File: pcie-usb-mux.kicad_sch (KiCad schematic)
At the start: 7 parts, among them U16 TMUXHS4212IRKSR

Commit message: [#83609] Reannotate board
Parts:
- renumbered C39 to C19, C40 to C20, C41 to C21, R159 to R95, R48 to R96, R49 to R97, U16 to U5
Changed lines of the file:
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@@
 		(on_board yes)
 		(dnp no)
-		(property "Reference" "#PWR068"
+		(property "Reference" "#PWR041"
 			(at 195.58 107.95 0)
 			(effects
@@
 			(project "bmc-reference-carrier-board"
 				(path "/5f636c45-3c15-4731-8931-4625e0dab7e4/02dc288a-88ee-45fa-83b7-00b3500b0ccd"
-					(reference "#PWR068")
+					(reference "#PWR041")
 					(unit 1)
 				)
@@
 		(on_board yes)
 		(dnp no)
-		(property "Reference" "#PWR070"
+		(property "Reference" "#PWR042"
 			(at 199.39 158.75 0)
 			(effects
@@
 			(project "bmc-reference-carrier-board"
 				(path "/5f636c45-3c15-4731-8931-4625e0dab7e4/02dc288a-88ee-45fa-83b7-00b3500b0ccd"
-					(reference "#PWR070")
+					(reference "#PWR042")
 					(unit 1)
 				)
@@
 		(on_board yes)
 		(dnp no)
-		(property "Reference" "#PWR066"
+		(property "Reference" "#PWR038"
 			(at 176.53 107.95 0)
 			(effects
@@
 			(project "bmc-reference-carrier-board"
 				(path "/5f636c45-3c15-4731-8931-4625e0dab7e4/02dc288a-88ee-45fa-83b7-00b3500b0ccd"
-					(reference "#PWR066")
+					(reference "#PWR038")
 					(unit 1)
 				)
@@
 		(on_board yes)
 		(dnp no)
-		(property "Reference" "#PWR069"
+		(property "Reference" "#PWR040"
 			(at 189.23 158.75 0)
 			(effects
@@
 			(project "bmc-reference-carrier-board"
 				(path "/5f636c45-3c15-4731-8931-4625e0dab7e4/02dc288a-88ee-45fa-83b7-00b3500b0ccd"
-					(reference "#PWR069")
+					(reference "#PWR040")
 					(unit 1)
 				)
@@
 		(dnp no)
 		(fields_autoplaced yes)
-		(property "Reference" "U16"
+		(property "Reference" "U5"
 			(at 209.55 105.41 0)
 			(effects
@@
 			(project ""
 				(path "/5f636c45-3c15-4731-8931-4625e0dab7e4/02dc288a-88ee-45fa-83b7-00b3500b0ccd"
-					(reference "U16")
+					(reference "U5")
 					(unit 1)
 				)
@@
 		(on_board yes)
 		(dnp no)
-		(property "Reference" "#PWR065"
+		(property "Reference" "#PWR043"
 			(at 213.36 149.86 0)
 			(effects
@@
 			(project ""
 				(path "/5f636c45-3c15-4731-8931-4625e0dab7e4/02dc288a-88ee-45fa-83b7-00b3500b0ccd"
-					(reference "#PWR065")
+					(reference "#PWR043")
 					(unit 1)
 				)
@@
 		(dnp no)
 		(fields_autoplaced yes)
-		(property "Reference" "C39"
+		(property "Reference" "C19"
 			(at 170.18 100.3236 90)
 			(effects
@@
 			(project ""
 				(path "/5f636c45-3c15-4731-8931-4625e0dab7e4/02dc288a-88ee-45fa-83b7-00b3500b0ccd"
-					(reference "C39")
+					(reference "C19")
 					(unit 1)
 				)
@@
 		(on_board yes)
 		(dnp no)
-		(property "Reference" "#PWR067"
+		(property "Reference" "#PWR039"
 			(at 186.69 107.95 0)
 			(effects
@@
 			(project "bmc-reference-carrier-board"
 				(path "/5f636c45-3c15-4731-8931-4625e0dab7e4/02dc288a-88ee-45fa-83b7-00b3500b0ccd"
-					(reference "#PWR067")
+					(reference "#PWR039")
 					(unit 1)
 				)
@@
 		(dnp no)
 		(fields_autoplaced yes)
-		(property "Reference" "C41"
+		(property "Reference" "C21"
 			(at 189.23 100.3236 90)
 			(effects
@@
 			(project "bmc-reference-carrier-board"
 				(path "/5f636c45-3c15-4731-8931-4625e0dab7e4/02dc288a-88ee-45fa-83b7-00b3500b0ccd"
-					(reference "C41")
+					(reference "C21")
 					(unit 1)
 				)
@@
 		(dnp no)
 		(fields_autoplaced yes)
-		(property "Reference" "C40"
+		(property "Reference" "C20"
 			(at 180.34 100.3236 90)
 			(effects
@@
 			(project "bmc-reference-carrier-board"
 				(path "/5f636c45-3c15-4731-8931-4625e0dab7e4/02dc288a-88ee-45fa-83b7-00b3500b0ccd"
-					(reference "C40")
+					(reference "C20")
 					(unit 1)
 				)
@@
 		(dnp no)
 		(fields_autoplaced yes)
-		(property "Reference" "#PWR0201"
+		(property "Reference" "#PWR037"
 			(at 182.88 96.52 0)
 			(effects
@@
 			(project ""
 				(path "/5f636c45-3c15-4731-8931-4625e0dab7e4/02dc288a-88ee-45fa-83b7-00b3500b0ccd"
-					(reference "#PWR0201")
+					(reference "#PWR037")
 					(unit 1)
 				)
@@
 		(on_board yes)
 		(dnp no)
-		(property "Reference" "R159"
+		(property "Reference" "R95"
 			(at 170.815 142.24 0)
 			(effects
@@
 			(project ""
 				(path "/5f636c45-3c15-4731-8931-4625e0dab7e4/02dc288a-88ee-45fa-83b7-00b3500b0ccd"
-					(reference "R159")
+					(reference "R95")
 					(unit 1)
 				)
@@
 		(on_board yes)
 		(dnp no)
-		(property "Reference" "R49"
+		(property "Reference" "R97"
 			(at 191.77 151.13 90)
 			(effects
@@
 			(project "bmc-reference-carrier-board"
 				(path "/5f636c45-3c15-4731-8931-4625e0dab7e4/02dc288a-88ee-45fa-83b7-00b3500b0ccd"
-					(reference "R49")
+					(reference "R97")
 					(unit 1)
 				)
@@
 		(on_board yes)
 		(dnp no)
-		(property "Reference" "R48"
+		(property "Reference" "R96"
 			(at 181.864 151.13 90)
 			(effects
@@
 			(project ""
 				(path "/5f636c45-3c15-4731-8931-4625e0dab7e4/02dc288a-88ee-45fa-83b7-00b3500b0ccd"
-					(reference "R48")
+					(reference "R96")
 					(unit 1)
 				)

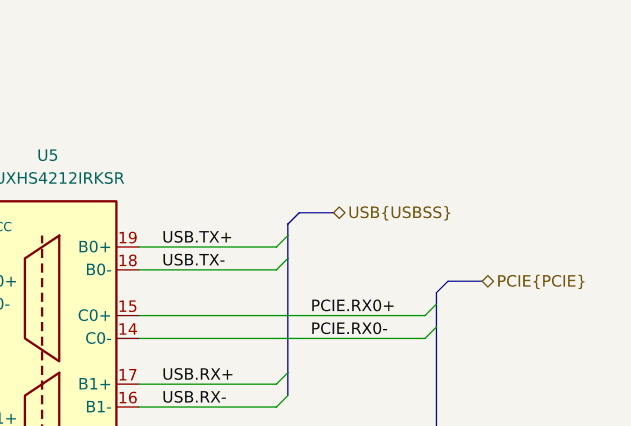
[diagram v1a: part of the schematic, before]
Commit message: [#83767] Add USB SS RX/TX swap note
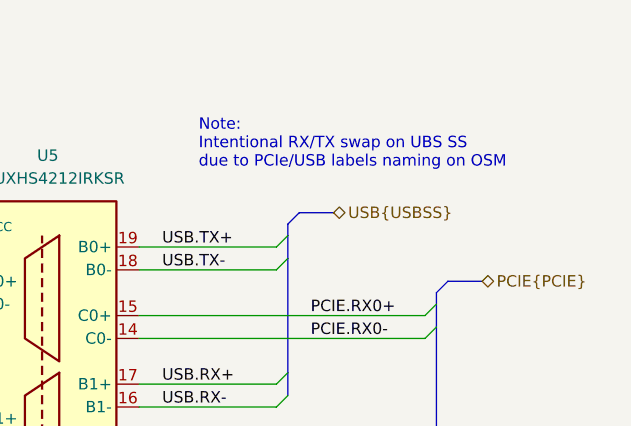
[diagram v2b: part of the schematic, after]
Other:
- note added: "Note: Intentional RX/TX swap on UBS SS due to PCIe/USB labels naming on OSM"
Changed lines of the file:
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@@
 		(rev "1.0.0")
+	)
+	(text "Note:\nIntentional RX/TX swap on UBS SS\ndue to PCIe/USB labels naming on OSM"
+		(exclude_from_sim no)
+		(at 226.314 104.14 0)
+		(effects
+			(font
+				(size 1.27 1.27)
+			)
+			(justify left)
+		)
 	)
 	(junction

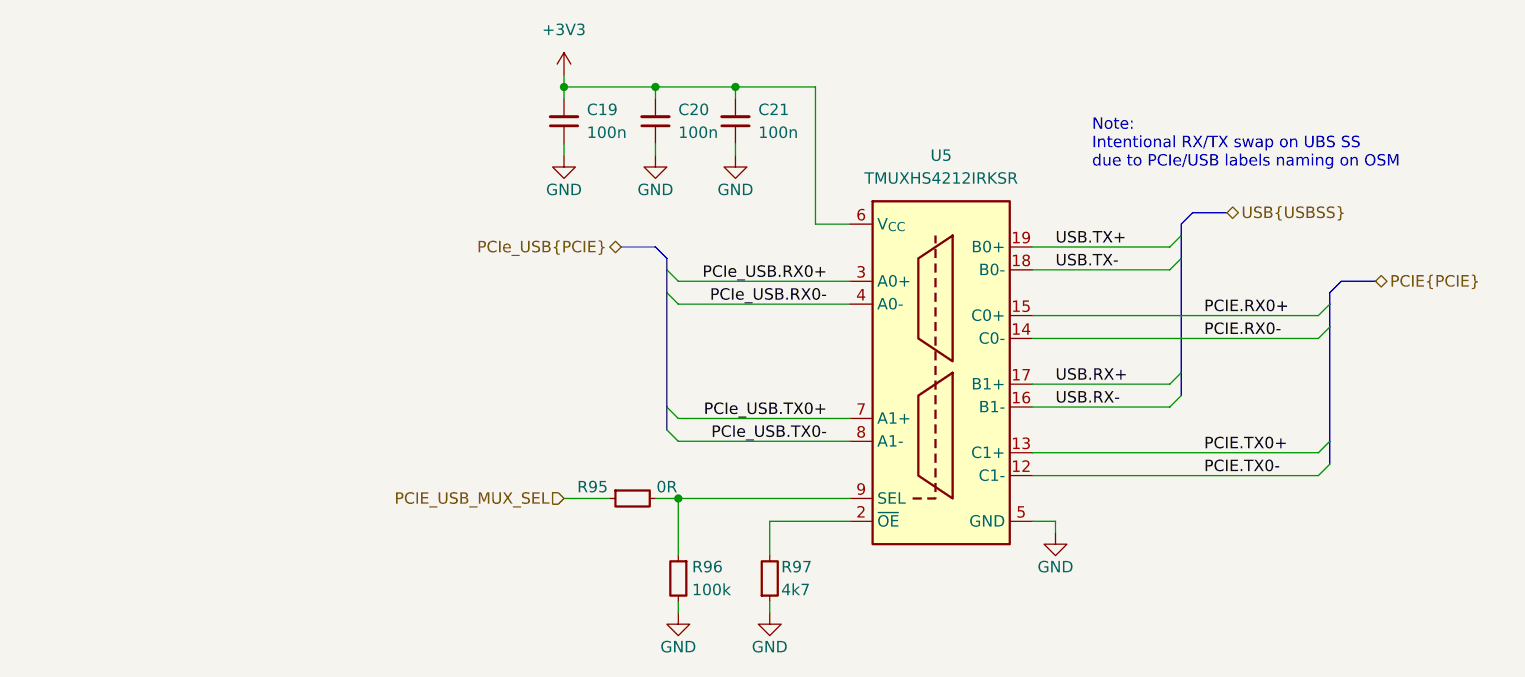
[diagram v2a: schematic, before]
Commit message: [#83767] Fix U5 SEL signal voltage
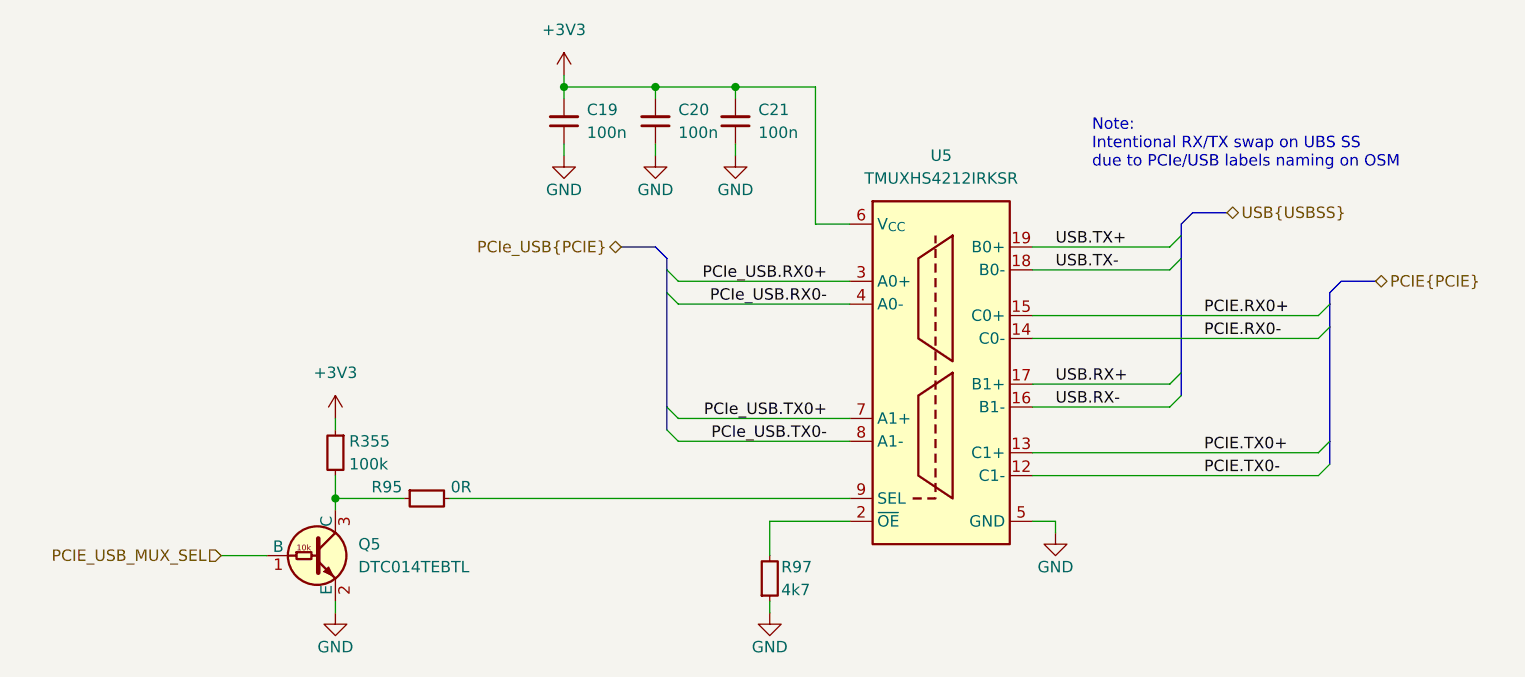
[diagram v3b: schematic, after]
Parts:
- removed R96: R_100k_0402, antmicro-footprints:R_0402_1005Metric, symbol antmicroResistors0402:R_100k_0402
- added Q5: DTC014T_SOT-416, antmicro-footprints:SOT-416, symbol antmicroTransistorsBipolarSingle:DTC014T_SOT-416
- added R355: R_100k_0402, antmicro-footprints:R_0402_1005Metric, symbol antmicroResistors0402:R_100k_0402
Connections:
- net +3V3: now also R355.1
- net GND: now also Q5.2 (E)
- net PCIE_USB_MUX_SEL: now also Q5.1 (B); no longer R95.1
- new net: Q5.3 (C), R355.2, R95.1
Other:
- moved on the sheet: R95

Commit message: [#83767] Reduce TMUXHS4212IRKSR decoupling
Datasheet suggests 100nF
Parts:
- removed C20, C21: C_100n_0402, antmicro-footprints:C_0402_1005Metric, symbol antmicroCapacitors0402:C_100n_0402
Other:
- moved on the sheet: C19
